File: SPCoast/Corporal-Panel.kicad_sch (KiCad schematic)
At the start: 17 parts, among them U12031 0x2A, U12032 0x2B

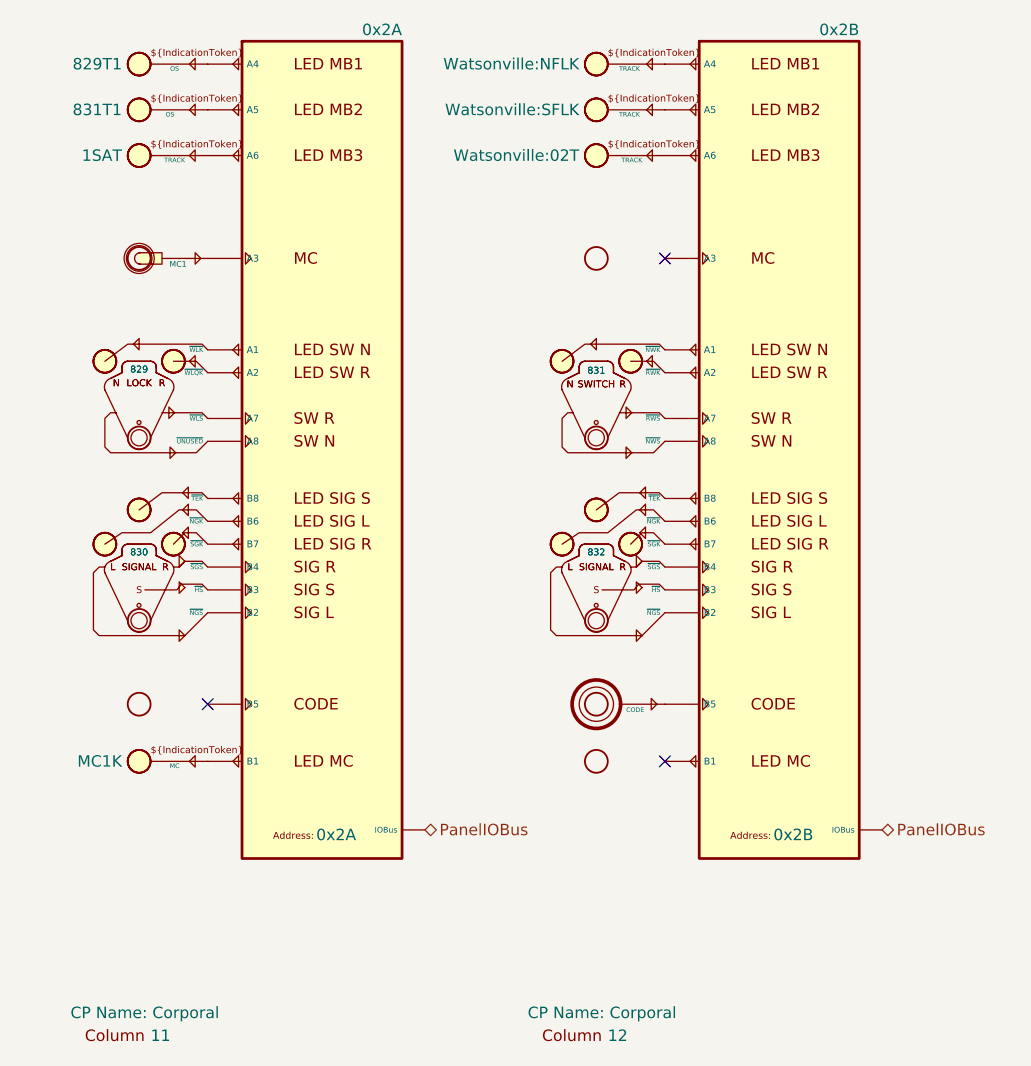
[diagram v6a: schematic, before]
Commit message: feat(spcoast): per-pin token fields on the panels, lamp Indication expressions, maintainer calls named 1MC
Applies the symbol rulings of 2026-10-28 to every sheet: the lib_symbols
caches of the changed symbols are the library's copies (this also clears
the stale PanelMCall and MaintainerCall caches), and every placed
instance gets the new hidden Control.*/Indication.* fields, loses
PanelLock Invert, and PanelMCall's whole-symbol Control and Indication
(Pin.MCK binary). Model lamps' IndicationToken becomes Indication: each
comma-separated circuit gets its K, qualifiers kept, joined with " | "
(795T1,01T,799T1 -> 795T1K | 01TK | 799T1K).

Maintainer calls in Christopher (1, 2), Corporal, Luchessa and Sargent
follow Gilroy Interchange (5dad54f): Value MC<n> -> <n>, Name ${Value}MC,
and the separate PanelMCall-Lamp is replaced by unit 2 of the same
PanelMCall at the old lamp's position, so its MCK pin sits where the
LAMP pin was. The old lamps' Column pin touched PanelColumn pin 8
directly (no wire); that pin is now unconnected, as on Gilroy
Interchange. Gilroy Interchange's local MaintainerCall_1 cache and its
two trackplan calls lose Indication.

Verified: fresh netlist before/after: components 752 -> 747 (the five
lamps), nets 1028 -> 1028; each old LAMP-pin net now holds the lever's
unit-2 MCK pin (pin 3) on the same expander pin (B1, pin 9); the levers'
nets are renamed only (~{S} -> ~{MCS}, unit suffix A); no other net
changed. Every field difference is an intended one. ERC 18 -> 1
violations (lib_symbol_mismatch 17 -> 0; pre-existing Sargent AUX1
pin_not_connected remains).

Co-Authored-By: Claude Opus 5.5 <noreply@anthropic.com>
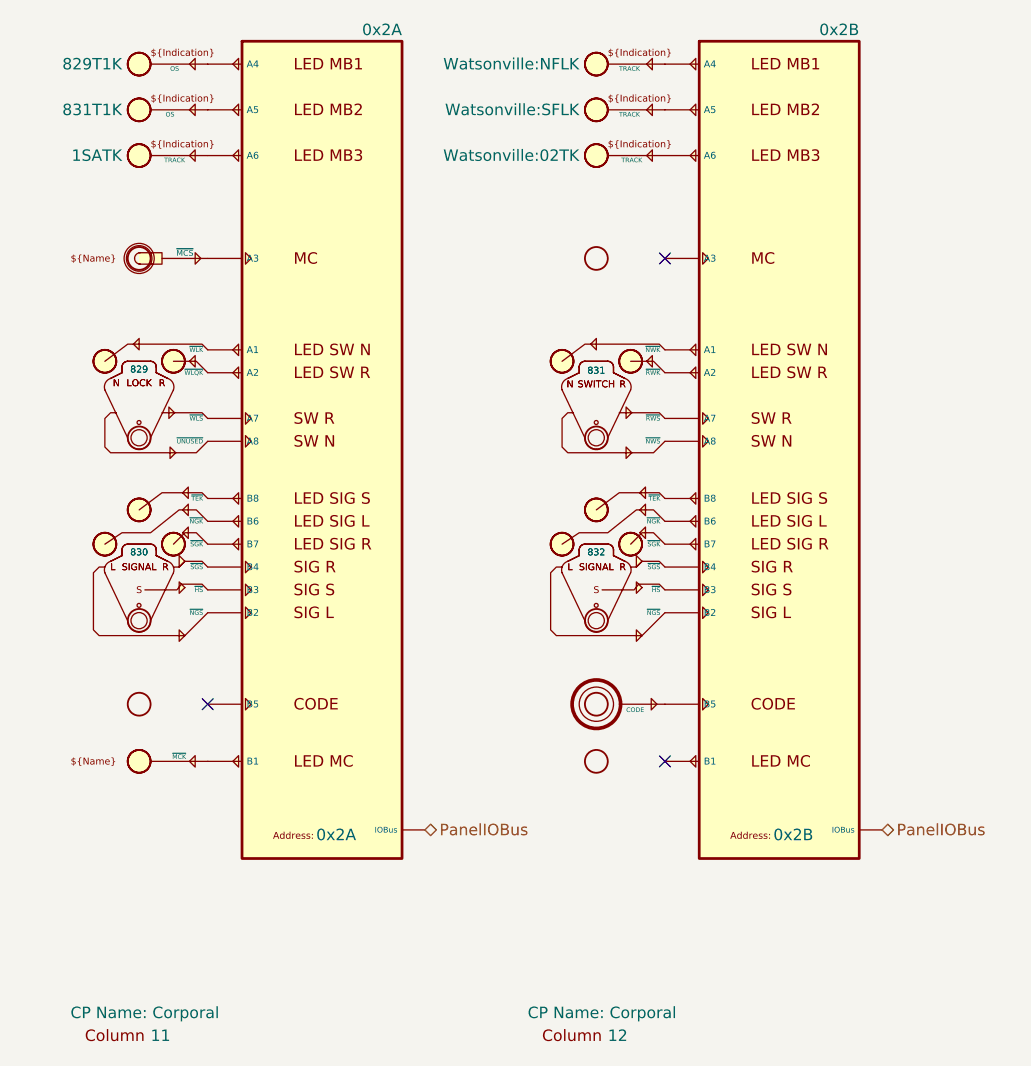
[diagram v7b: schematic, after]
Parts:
- removed MCK12011: MC, symbol Railroad-Office:PanelMCall-Lamp
- added unit 2 of MCL12011
- LKL12011: Control.WLS (none) -> ${Value}WLS; Indication.WLK (none) -> !${Value}WLK; Indication.WLQK (none) -> ${Value}WLQK; Invert WLK -> (none)
- LMP12111: Indication (none) -> 829T1K; IndicationToken 829T1 -> (none)
- LMP12112: Indication (none) -> 831T1K; IndicationToken 831T1 -> (none)
- LMP12113: Indication (none) -> 1SATK; IndicationToken 1SAT -> (none)
- LMP12121: Indication (none) -> Watsonville:NFLK; IndicationToken Watsonville:NFLK -> (none)
- LMP12122: Indication (none) -> Watsonville:SFLK; IndicationToken Watsonville:SFLK -> (none)
- LMP12123: Indication (none) -> Watsonville:02TK; IndicationToken Watsonville:02T -> (none)
- MCL12011: value MC1 -> 1; Control.MCS (none) -> ${Value}MCS; Indication.MCK (none) -> ${Value}MCK; Name ${Value} -> ${Value}MC; Pin.MCK (none) -> binary; Pin.MCS (none) -> binary; Pin.S binary -> (none)
- SGL12011, SGL12012: Control.HS (none) -> ${Value}HS; Control.NGS (none) -> ${Value}NGS; Control.SGS (none) -> ${Value}SGS; Indication.NGK (none) -> ${Value}NGK; Indication.SGK (none) -> ${Value}SGK; Indication.TEK (none) -> ${Value}TEK
- SWL12012: Control.NWS (none) -> ${Value}NWS; Control.RWS (none) -> ${Value}RWS; Indication.NWK (none) -> ${Value}NWK; Indication.RWK (none) -> ${Value}RWK
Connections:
- net at U12031.9 (B1): now also MCL12011.3 (~{MCK})
